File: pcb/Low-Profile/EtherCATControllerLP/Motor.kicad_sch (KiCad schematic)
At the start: 15 parts, among them U6 MCF8329A1IREER

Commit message: checkpoint
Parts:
- C20, C21, C22, C23, C25: footprint (none) -> 0603; LCSC Part # (none) -> C106858
- C24: value C_Small -> 1uF; footprint (none) -> 0603; LCSC Part # (none) -> C106858
- C26: footprint (none) -> 0805; LCSC Part # (none) -> C28233
- C27: LCSC Part # (none) -> C506619
- C28: footprint (none) -> 0603; LCSC Part # (none) -> C107062
- R11, R12, R13, R14: footprint (none) -> 0402; LCSC Part # (none) -> C105872
- U6: footprint WQFN36_REE_TEX -> (none); LCSC Part # (none) -> C22399784; LCSC Part Number C22399784 -> (none)
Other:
- note added: "Tant Cap"
- note removed: "Bulk Cap"

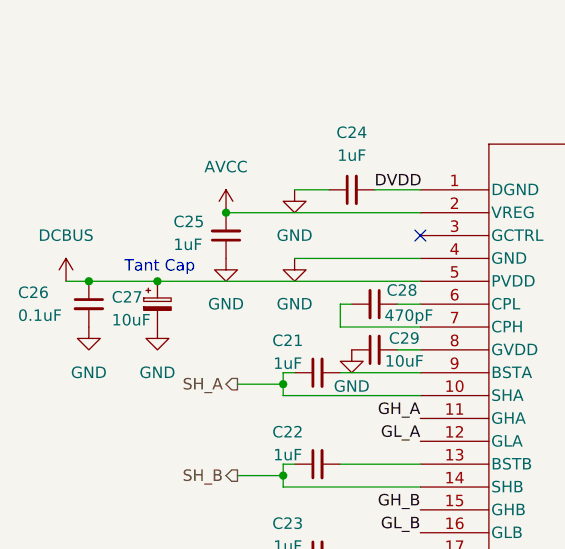
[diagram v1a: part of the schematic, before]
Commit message: Checkpoint changes before switching to XMC4800
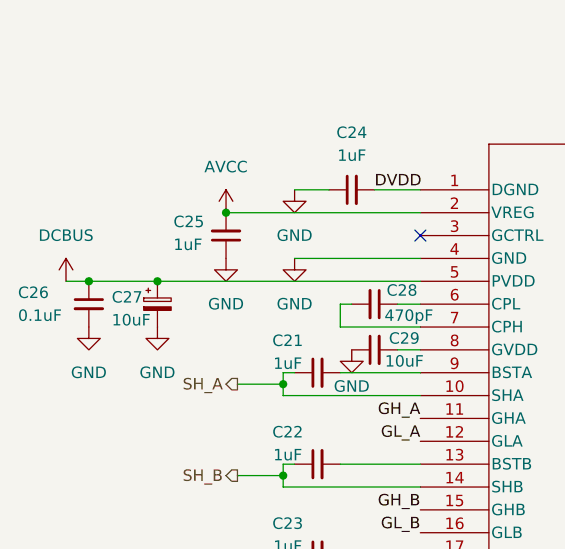
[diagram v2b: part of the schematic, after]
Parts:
- C27: footprint (none) -> SMD D6.3x5.4; LCSC Part # C506619 -> C2977481
- C29: LCSC Part # (none) -> C194427
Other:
- note removed: "Tant Cap"
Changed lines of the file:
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@@
-		)
-	)
-	(text "Tant Cap"
-		(exclude_from_sim no)
-		(at 40.894 79.756 0)
-		(effects
-			(font
-				(size 1.27 1.27)
-			)
 		)
 	)
@@
 			)
 		)
+		(property "LCSC Part #" "C194427"
+			(at 64.77 88.9 0)
+			(effects
+				(font
+					(size 1.27 1.27)
+				)
+				(hide yes)
+			)
+		)
 		(pin "2"
 		)
@@
 			)
 		)
-		(property "Footprint" ""
+		(property "Footprint" "SMD D6.3x5.4"
 			(at 40.64 83.82 0)
 			(effects
@@
 			)
 		)
-		(property "LCSC Part #" "C506619"
+		(property "LCSC Part #" " C2977481"
 			(at 40.64 83.82 0)
 			(effects
